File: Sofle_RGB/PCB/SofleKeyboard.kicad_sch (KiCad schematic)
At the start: 95 parts, among them J1 LED, J2 4PIN, J3 OLED, J4 key leds, J5 backlight sel, J6 indicator bypass, P1 i2c_pin, P2 i2c_pin, SW1 SW_PUSH-MX_W_LED, SW10 SW_PUSH-MX_W_LED, SW11 SW_PUSH-MX_W_LED, SW12 SW_PUSH-MX_W_LED, SW13 SW_PUSH-MX_W_LED, SW14 SW_PUSH-MX_W_LED, SW15 SW_PUSH-MX_W_LED, SW16 SW_PUSH-MX_W_LED, SW17 SW_PUSH-MX_W_LED, SW18 SW_PUSH-MX_W_LED, SW19 SW_PUSH-MX_W_LED, SW2 SW_PUSH-MX_W_LED, SW20 SW_PUSH-MX_W_LED, SW21 SW_PUSH-MX_W_LED, SW22 SW_PUSH-MX_W_LED, SW23 SW_PUSH-MX_W_LED, SW24 SW_PUSH-MX_W_LED, SW25 Rotary_Encoder_Switch, SW26 SW_PUSH-MX_W_LED, SW27 SW_PUSH-MX_W_LED, SW28 SW_PUSH-MX_W_LED, SW29 SW_PUSH-MX_W_LED, SW3 SW_PUSH-MX_W_LED, SW30 SW_PUSH-MX_W_LED, SW4 SW_PUSH-MX_W_LED, SW5 SW_PUSH-MX_W_LED, SW6 SW_PUSH-MX_W_LED, SW7 SW_PUSH-MX_W_LED, SW8 SW_PUSH-MX_W_LED, SW9 SW_PUSH-MX_W_LED, U1 ProMicro

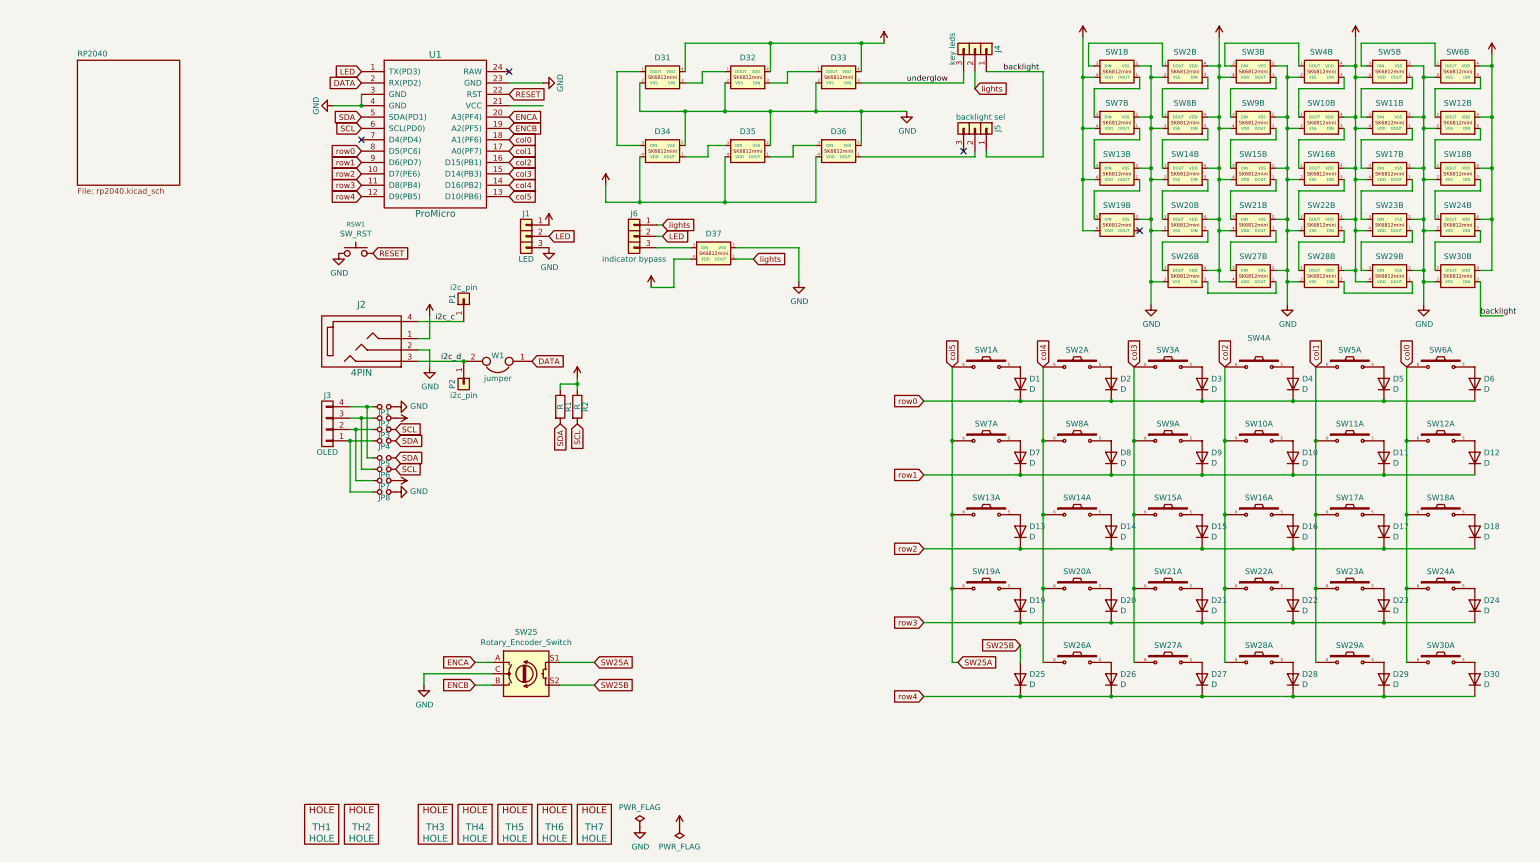
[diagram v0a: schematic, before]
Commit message: RP2040 schematic: - Added Reset and Boot button - Added Crystal - Added Flash - Added (optional) LED level shifter - Rearanged schematic
Main schematic:
- Imported Pins from rp2040 schematic
- Replaced VCC with VBUS representing USB voltage
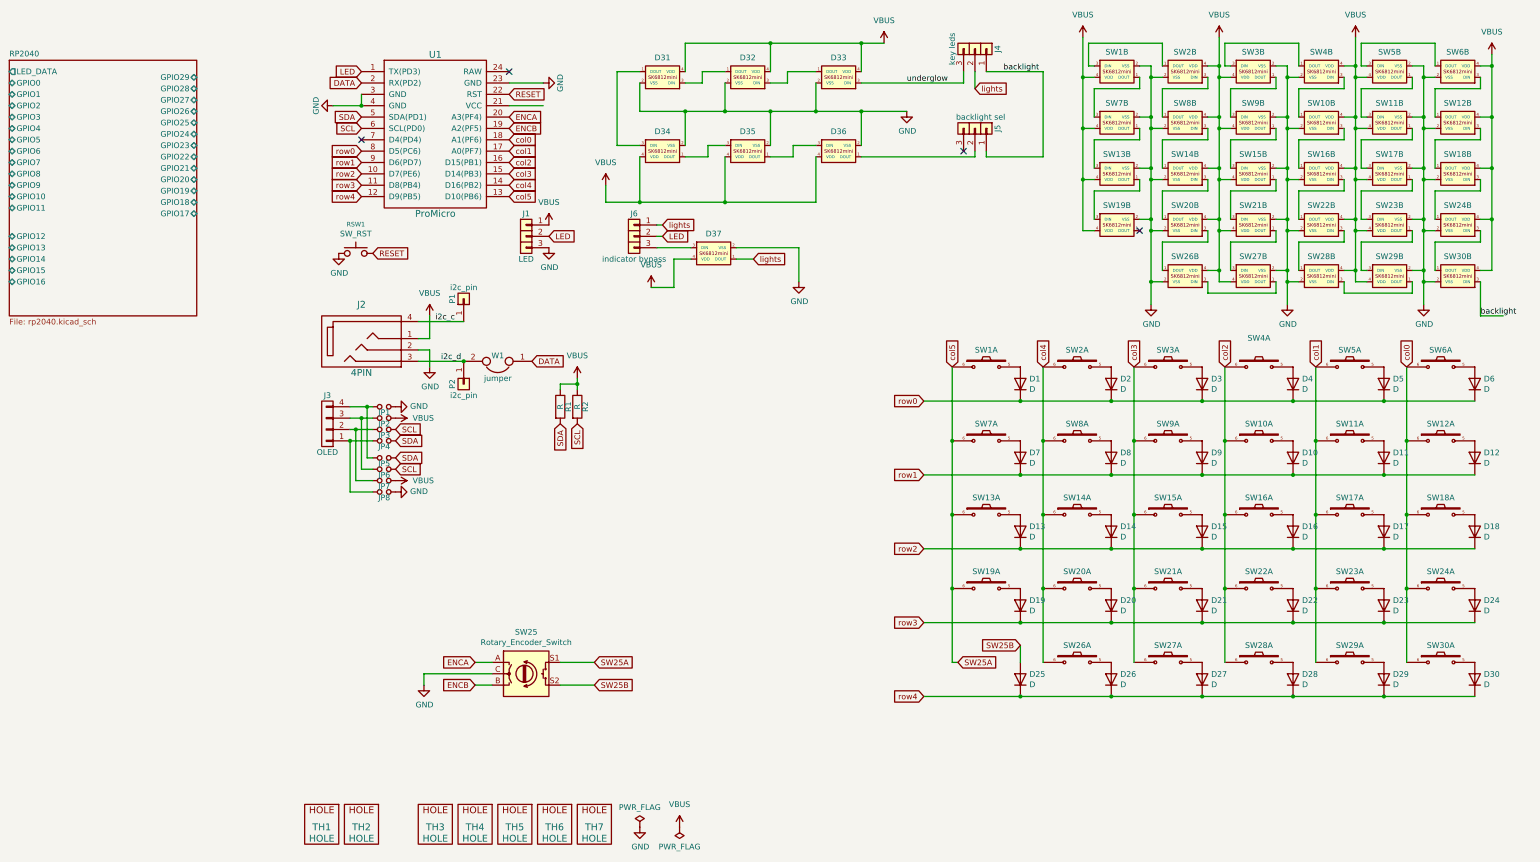
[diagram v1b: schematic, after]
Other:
- sheet RP2040 ports: added GPIO0, GPIO1, GPIO10, GPIO11, GPIO12, GPIO13, GPIO14, GPIO15, GPIO16, GPIO17, GPIO18, GPIO19, GPIO2, GPIO20, GPIO21, GPIO22, GPIO23, GPIO24, GPIO25, GPIO26, GPIO27, GPIO28, GPIO29, GPIO3, GPIO4, GPIO5, GPIO6, GPIO7, GPIO8, GPIO9, LED_DATA; removed none
